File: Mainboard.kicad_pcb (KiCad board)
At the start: 4 copper layers, 100 x 60 mm, 314 parts, among them J1 USB_B_Micro, J10 Conn_01x02_Male, J11 Conn_01x02_Male, J12 Conn_01x02_Male, J2 8P8C_LED, J3 Micro_SD_Card_Det, J4 Conn_Coaxial, J5 Conn_Coaxial, J6 Screw_Terminal_01x02, J7 Screw_Terminal_01x02, J8 Screw_Terminal_01x02, J9 Conn_01x02_Male, Q1 MMDT2222A, Q3 PMV20ENR, Q4 PMV20ENR, Q5 PMV20ENR, U1 CP2102N-A01-GQFN24, U10 LTV-817S, U11 RFM95W-868S2, U2 SN65HVD230, U3 ESP32-WROOM-32D, U4 W25Q64FV, U5 MS5607-02BA, U6 MAX-M8Q, U7 LSM9DS1, U8 TPS63031, U9 LTV-817S

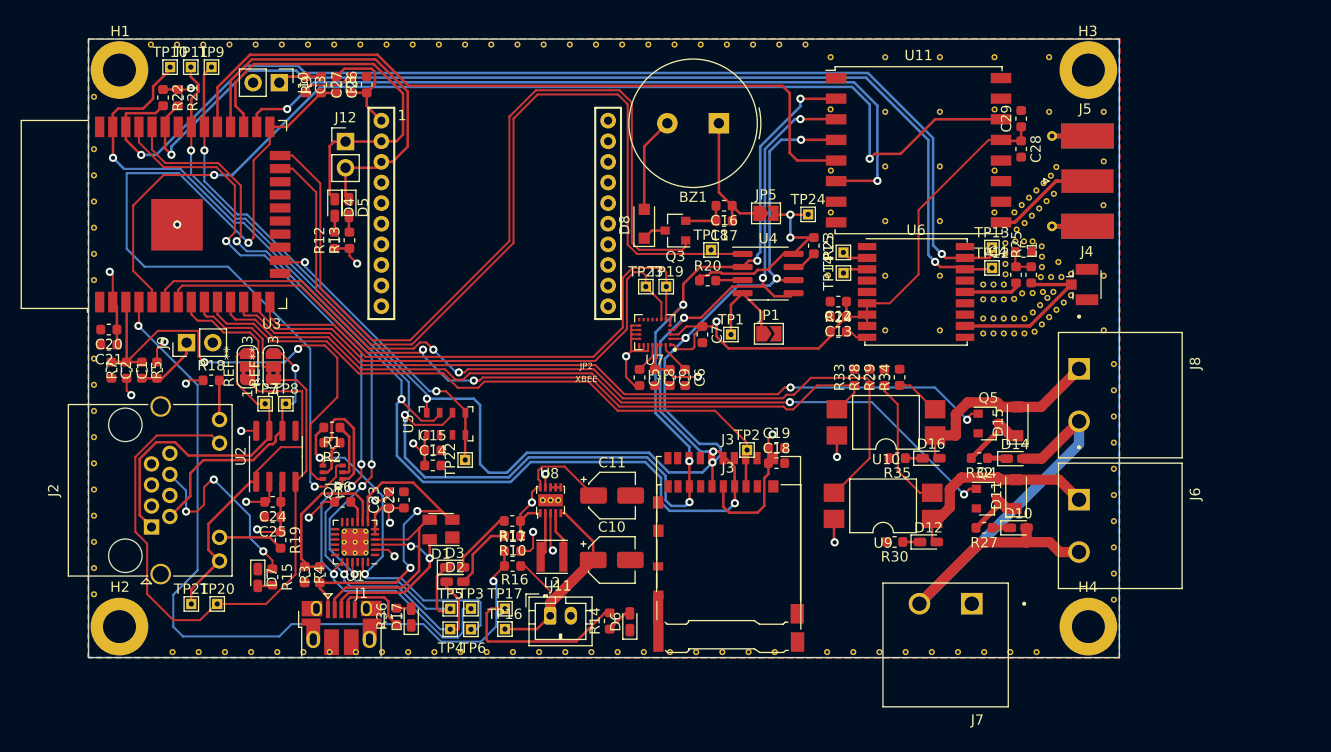
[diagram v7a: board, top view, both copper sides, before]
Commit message: finished silkscreen
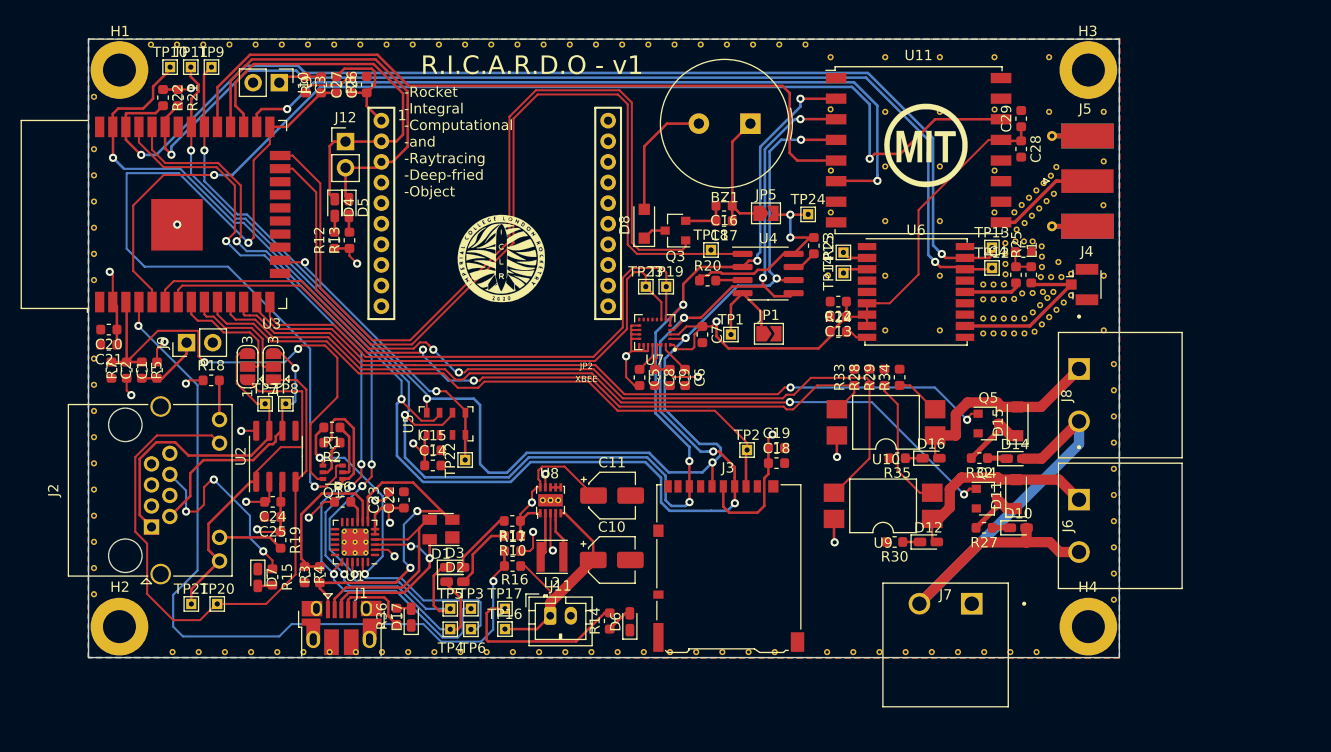
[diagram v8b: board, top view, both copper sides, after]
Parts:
- removed the J3 at (147.1, 98.4)
- added G***: LOGO, iclr-hw:ricardo_logo, F.Cu at (138.1, 80.0)
- added G***: LOGO, iclr-hw:iclr_logo, F.Cu at (125.0, 71.3)
- added G***: LOGO, iclr-hw:MIT_logo, F.Cu at (166.2, 60.3)
- added REF**: Write_Pad, iclr-hw:Write_Pad, F.Cu at (110.0, 80.0)
- REF** (x2): value SolderJumper-3_P1.3mm_Bridged2Bar12_RoundedPad1.0x1.5mm_NumberLabels -> SolderJumper-3_P1.3mm_Open_RoundedPad1.0x1.5mm; footprint Jumper:SolderJumper-3_P1.3mm_Bridged2Bar12_RoundedPad1.0x1.5mm_NumberLabels -> Jumper:SolderJumper-3_P1.3mm_Open_RoundedPad1.0x1.5mm
- moved BZ1 3.06 mm to (149.2, 58.2)
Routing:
- net Net-(BZ1-Pad2): track 9.28 -> 12.3 mm
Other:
- board text added: "-Rocket -Integral -Computational -and -Raytracing -Deep-fried -Object"
- board text added: "Designed By - Kiran de Silva"
- board text added: "ICLR Electronics & Payload"
- board text added: "R.I.C.A.R.D.O - v1"
- board text added: "RICARDO"
